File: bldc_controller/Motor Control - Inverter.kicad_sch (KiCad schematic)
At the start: 42 parts, among them J3 Phase A, J4 Phase B, J5 Phase C, Q1 TPW1R306PL,L1Q, Q2 TPW1R306PL,L1Q, Q3 TPW1R306PL,L1Q, Q4 TPW1R306PL,L1Q, Q5 TPW1R306PL,L1Q, Q6 TPW1R306PL,L1Q

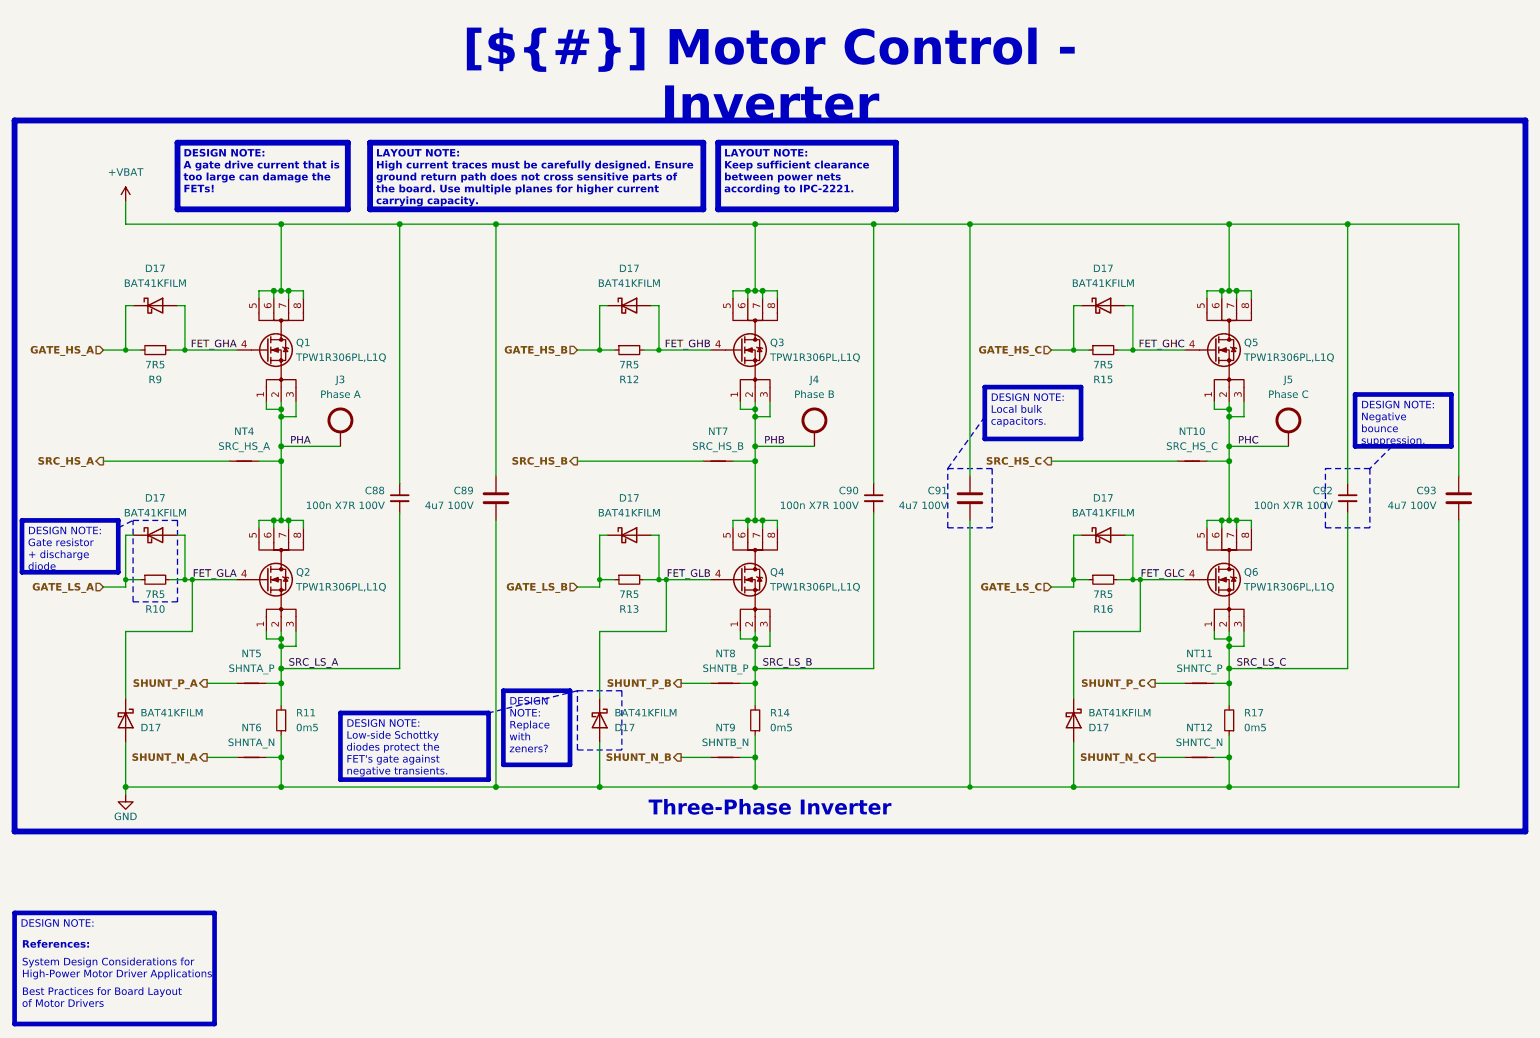
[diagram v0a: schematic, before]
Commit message: schematic is complete. Replaced 5V buck and added pi filters.
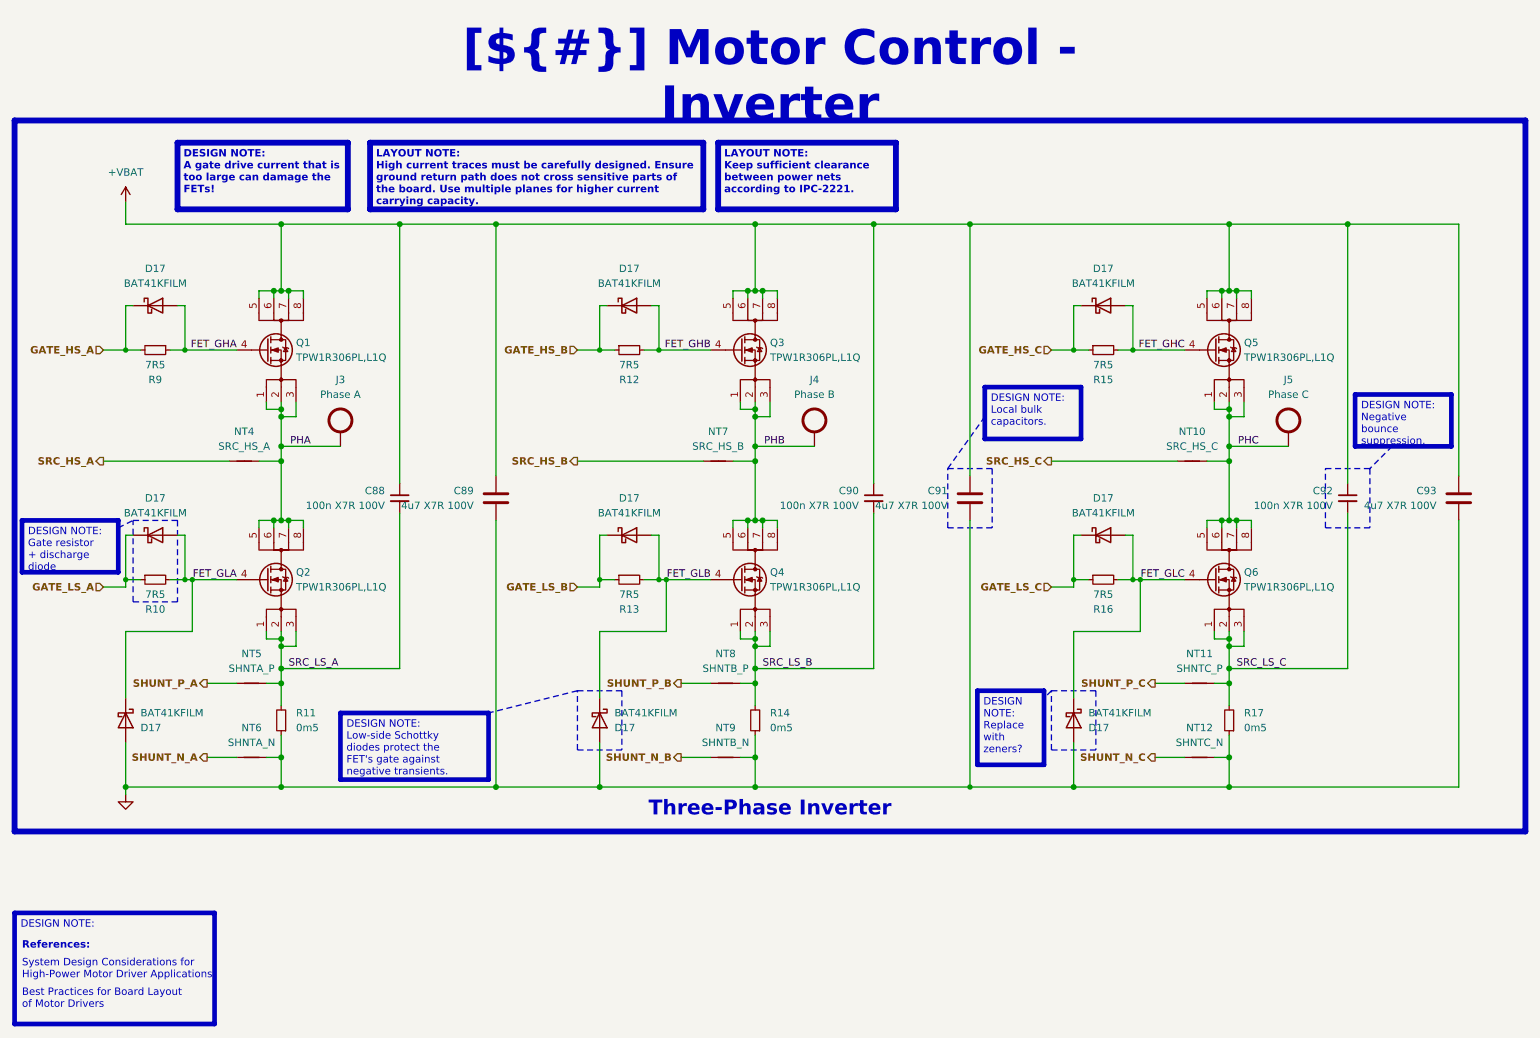
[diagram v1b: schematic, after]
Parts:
- C89, C91, C93: value 4u7 100V -> 4u7 X7R 100V
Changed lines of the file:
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@@
     (stroke (width 0.381) (type default) (color 160 30 210 1))
+  )
+  (polyline (pts (xy 196.85 128.27) (xy 195.58 129.54))
+    (stroke (width 0) (type dot) (color 255 0 0 1))
   )
   (wire (pts (xy 143.51 119.38) (xy 146.05 119.38))
@@
   )
   (rectangle (start 39.37 99.06) (end 46.99 113.03)
+    (stroke (width 0) (type dot) (color 255 0 0 1))
+    (fill (type none))
+  )
+  (rectangle (start 196.85 128.27) (end 204.47 138.43)
     (stroke (width 0) (type dot) (color 255 0 0 1))
     (fill (type none))
@@
   )
   (text_box "DESIGN NOTE:\nReplace with zeners?"
-    (at 102.87 128.27 0) (size 11.43 12.7)
+    (at 184.15 128.27 0) (size 11.43 12.7)
     (stroke (width 0.8) (type solid) (color 255 165 0 1))
     (fill (type none))
@@
     (effects (font (face "Arial") (size 1.27 1.27) (thickness 0.254) bold) (justify right))
   )
+  (netclass_flag "" (length 2.54) (shape round) (at 85.09 124.46 180)
+    (effects (font (face "Arial") (size 1.27 1.27)) (justify right bottom))
+    (property "Netclass" "High Power" (at 85.09 129.54 0) (show_name)
+      (effects (font (face "Arial") (size 1.27 1.27) italic (color 162 22 34 1)))
+    )
+  )
   (netclass_flag "" (length 2.54) (shape round) (at 134.62 139.7 180) (fields_autoplaced)
     (effects (font (face "Arial") (size 1.27 1.27)) (justify right bottom))
@@
     )
   )
-  (netclass_flag "" (length 2.54) (shape round) (at 73.66 86.36 180)
-    (effects (font (face "Arial") (size 1.27 1.27)) (justify right bottom))
-    (property "High Power" "High Power" (at 73.66 91.44 0)
+  (netclass_flag "" (length 2.54) (shape round) (at 74.93 86.36 180)
+    (effects (font (face "Arial") (size 1.27 1.27)) (justify right bottom))
+    (property "Netclass" "High Power" (at 74.93 91.44 0) (show_name)
+      (effects (font (face "Arial") (size 1.27 1.27) italic (color 162 22 34 1)))
+    )
+  )
+  (netclass_flag "" (length 2.54) (shape round) (at 166.37 124.46 180)
+    (effects (font (face "Arial") (size 1.27 1.27)) (justify right bottom))
+    (property "Netclass" "High Power" (at 166.37 129.54 0) (show_name)
+      (effects (font (face "Arial") (size 1.27 1.27) italic (color 162 22 34 1)))
+    )
+  )
+  (netclass_flag "" (length 2.54) (shape round) (at 247.65 124.46 180)
+    (effects (font (face "Arial") (size 1.27 1.27)) (justify right bottom))
+    (property "Netclass" "High Power" (at 247.65 129.54 0) (show_name)
+      (effects (font (face "Arial") (size 1.27 1.27) italic (color 162 22 34 1)))
+    )
+  )
+  (netclass_flag "" (length 2.54) (shape round) (at 156.21 86.36 180)
+    (effects (font (face "Arial") (size 1.27 1.27)) (justify right bottom))
+    (property "Netclass" "High Power" (at 156.21 91.44 0) (show_name)
       (effects (font (face "Arial") (size 1.27 1.27) italic (color 162 22 34 1)))
     )
@@
     )
   )
-  (netclass_flag "" (length 2.54) (shape round) (at 154.94 86.36 180)
-    (effects (font (face "Arial") (size 1.27 1.27)) (justify right bottom))
-    (property "High Power" "High Power" (at 154.94 91.44 0)
+  (netclass_flag "" (length 2.54) (shape round) (at 237.49 86.36 180)
+    (effects (font (face "Arial") (size 1.27 1.27)) (justify right bottom))
+    (property "Netclass" "High Power" (at 237.49 91.44 0) (show_name)
       (effects (font (face "Arial") (size 1.27 1.27) italic (color 162 22 34 1)))
     )
@@
     )
   )
-  (netclass_flag "" (length 2.54) (shape round) (at 83.82 124.46 180)
-    (effects (font (face "Arial") (size 1.27 1.27)) (justify right bottom))
-    (property "High Power" "High Power" (at 83.82 129.54 0)
-      (effects (font (face "Arial") (size 1.27 1.27) italic (color 162 22 34 1)))
-    )
-  )
-  (netclass_flag "" (length 2.54) (shape round) (at 236.22 86.36 180)
-    (effects (font (face "Arial") (size 1.27 1.27)) (justify right bottom))
-    (property "High Power" "High Power" (at 236.22 91.44 0)
-      (effects (font (face "Arial") (size 1.27 1.27) italic (color 162 22 34 1)))
-    )
-  )
   (netclass_flag "" (length 2.54) (shape round) (at 53.34 127 180) (fields_autoplaced)
     (effects (font (face "Arial") (size 1.27 1.27)) (justify right bottom))
@@
     )
   )
-  (netclass_flag "" (length 2.54) (shape round) (at 246.38 124.46 180)
-    (effects (font (face "Arial") (size 1.27 1.27)) (justify right bottom))
-    (property "High Power" "High Power" (at 246.38 129.54 0)
-      (effects (font (face "Arial") (size 1.27 1.27) italic (color 162 22 34 1)))
-    )
-  )
   (netclass_flag "" (length 2.54) (shape round) (at 135.255 127 180) (fields_autoplaced)
     (effects (font (face "Arial") (size 1.27 1.27)) (justify right bottom))
     (property "Kelvin Diff Pair" "DIFFPAIR" (at 135.9535 129.54 0)
       (effects (font (face "Arial") (size 1.27 1.27) italic (color 162 22 34 1)) (justify left))
-    )
-  )
-  (netclass_flag "" (length 2.54) (shape round) (at 165.1 124.46 180)
-    (effects (font (face "Arial") (size 1.27 1.27)) (justify right bottom))
-    (property "High Power" "High Power" (at 165.1 129.54 0)
-      (effects (font (face "Arial") (size 1.27 1.27) italic (color 162 22 34 1)))
     )
   )
@@
       (effects (font (size 1.27 1.27)) (justify left))
     )
-    (property "Value" "4u7 100V" (at 97.79 96.52 0)
+    (property "Value" "4u7 X7R 100V" (at 97.79 96.52 0)
       (effects (font (size 1.27 1.27)) (justify left))
     )
@@
     )
     (property "Value" "GND" (at 38.1 149.86 0)
-      (effects (font (size 1.27 1.27)))
+      (effects (font (size 1.27 1.27)) hide)
     )
     (property "Footprint" "" (at 38.1 146.05 0)
@@
       (effects (font (size 1.27 1.27)) (justify left))
     )
-    (property "Value" "4u7 100V" (at 262.89 96.52 0)
+    (property "Value" "4u7 X7R 100V" (at 262.89 96.52 0)
       (effects (font (size 1.27 1.27)) (justify left))
     )
@@
       (effects (font (size 1.27 1.27)) (justify left))
     )
-    (property "Value" "4u7 100V" (at 179.07 96.52 0)
-      (effects (font (size 1.27 1.27)) (justify left))
-    )
+    (property "Value" "4u7 X7R 100V" (at 179.07 96.52 0)
+      (effects (font (size 1.27 1.27)) (justify left))
+    )

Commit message: added assembly files
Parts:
- R10, R12, R13, R15, R16, R9: value 7R5 -> 7R5 1%
- R11, R14, R17: value 0m5 -> 0m5 1% 2W
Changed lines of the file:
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@@
     (stroke (width 0) (type default))
   )
-  (polyline (pts (xy 115.57 128.27) (xy 100.33 132.08))
+  (polyline (pts (xy 115.57 128.27) (xy 99.06 132.08))
     (stroke (width 0) (type dot) (color 255 0 0 1))
   )
@@
   )
   (text_box "DESIGN NOTE:\nLow-side Schottky diodes protect the FET's gate against negative transients."
-    (at 74.93 132.08 0) (size 25.4 11.43)
+    (at 78.74 130.81 0) (size 20.32 12.7)
     (stroke (width 0.8) (type solid) (color 200 200 200 1))
     (fill (type none))
@@
       (effects (font (size 1.27 1.27)) (justify right))
     )
-    (property "Value" "0m5" (at 67.31 134.62 0)
+    (property "Value" "0m5 1% 2W" (at 67.31 134.62 0)
       (effects (font (size 1.27 1.27)) (justify right))
     )
@@
       (effects (font (size 1.27 1.27)))
     )
-    (property "Value" "7R5" (at 124.46 72.39 90)
+    (property "Value" "7R5 1%" (at 124.46 72.39 90)
       (effects (font (size 1.27 1.27)))
     )
@@
       (effects (font (size 1.27 1.27)))
     )
-    (property "Value" "7R5" (at 205.74 111.76 90)
+    (property "Value" "7R5 1%" (at 205.74 111.76 90)
       (effects (font (size 1.27 1.27)))
     )
@@
       (effects (font (size 1.27 1.27)) (justify right))
     )
-    (property "Value" "0m5" (at 229.87 134.62 0)
+    (property "Value" "0m5 1% 2W" (at 229.87 134.62 0)
       (effects (font (size 1.27 1.27)) (justify right))
     )
@@
       (effects (font (size 1.27 1.27)))
     )
-    (property "Value" "7R5" (at 43.18 72.39 90)
+    (property "Value" "7R5 1%" (at 43.18 72.39 90)
       (effects (font (size 1.27 1.27)))
     )
@@
       (effects (font (size 1.27 1.27)))
     )
-    (property "Value" "7R5" (at 43.18 111.76 90)
+    (property "Value" "7R5 1%" (at 43.18 111.76 90)
       (effects (font (size 1.27 1.27)))
     )
@@
       (effects (font (size 1.27 1.27)))
     )
-    (property "Value" "7R5" (at 124.46 111.76 90)
+    (property "Value" "7R5 1%" (at 124.46 111.76 90)
       (effects (font (size 1.27 1.27)))
     )
@@
       (effects (font (size 1.27 1.27)) (justify right))
     )
-    (property "Value" "0m5" (at 148.59 134.62 0)
+    (property "Value" "0m5 1% 2W" (at 148.59 134.62 0)
       (effects (font (size 1.27 1.27)) (justify right))
     )
@@
       (effects (font (size 1.27 1.27)))
     )
-    (property "Value" "7R5" (at 205.74 72.39 90)
-      (effects (font (size 1.27 1.27)))
-    )
+    (property "Value" "7R5 1%" (at 205.74 72.39 90)
+      (effects (font (size 1.27 1.27)))
+    )
